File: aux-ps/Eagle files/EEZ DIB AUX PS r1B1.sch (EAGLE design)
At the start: 107 parts, among them IC1 AMC6821SDBQR, IC2 VIPer35L, IC3 TL431, J1 PF0030/PC, J2 SWEB 8094 AU/GN, Q1 BTA26-600, Q2 BTA26-600, Q3 2N7002, Q4 2N7002, Q5 IRLL2705PBF, Q6 2N7002, SW1 DF62J12S2AHQA, X1 39-28-1063, X2 39-30-1039, X3 ZL231-16KG, X4 22-23-2031, X5 22-23-2021

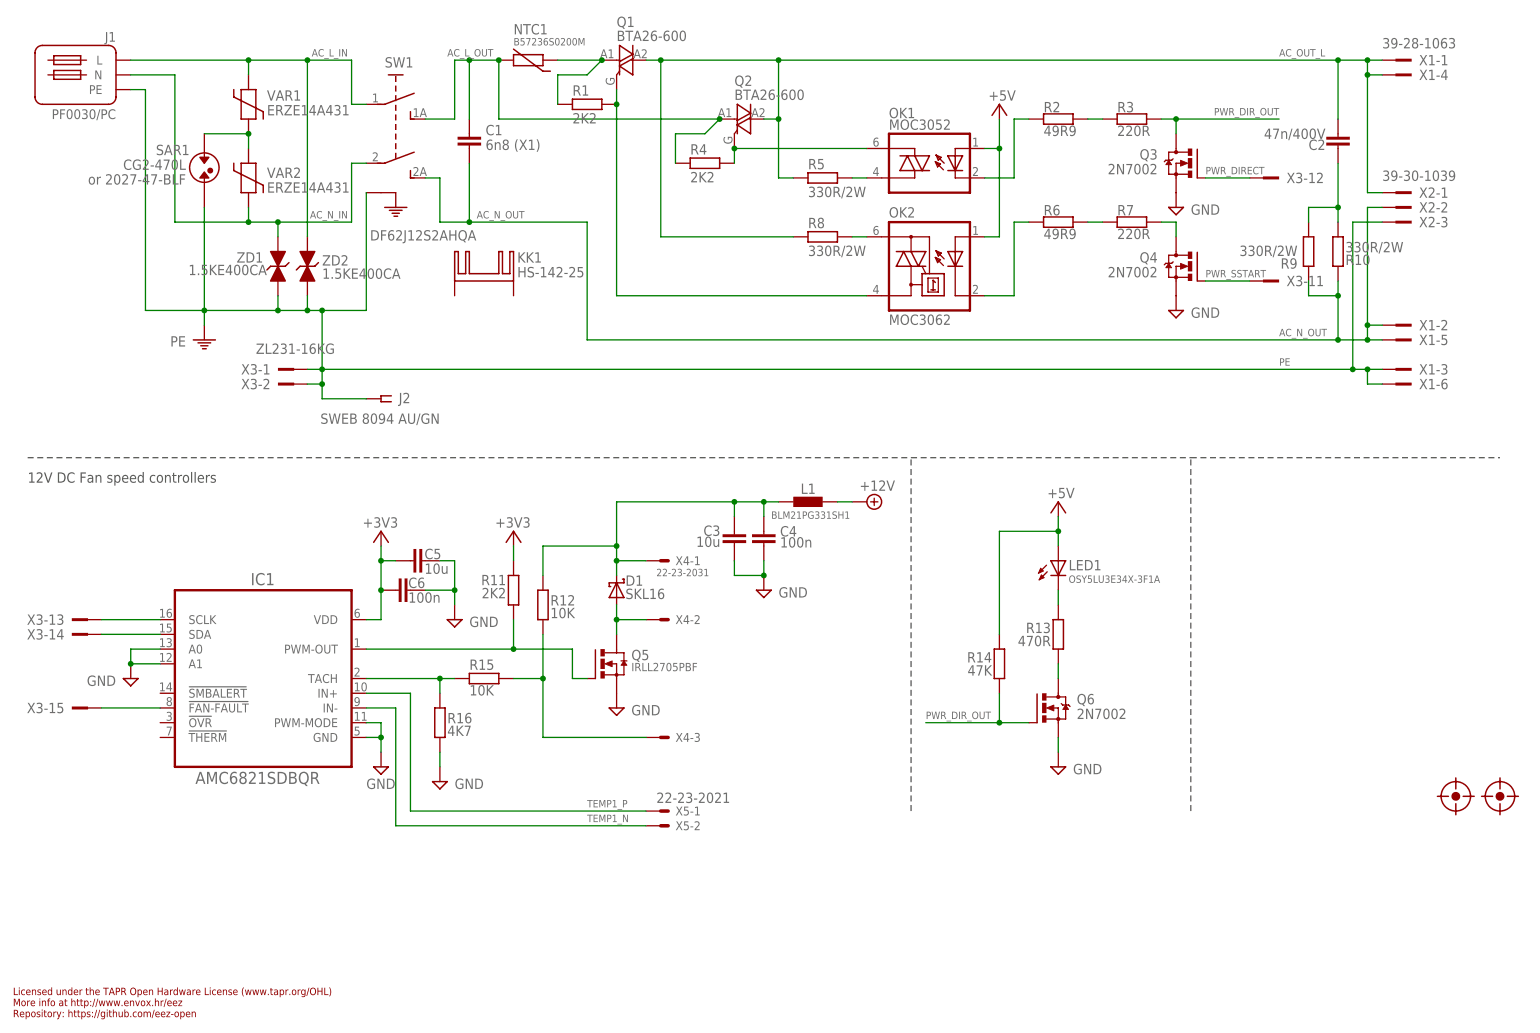
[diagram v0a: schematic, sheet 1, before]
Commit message: aux-ps BOM update, PE terminals added
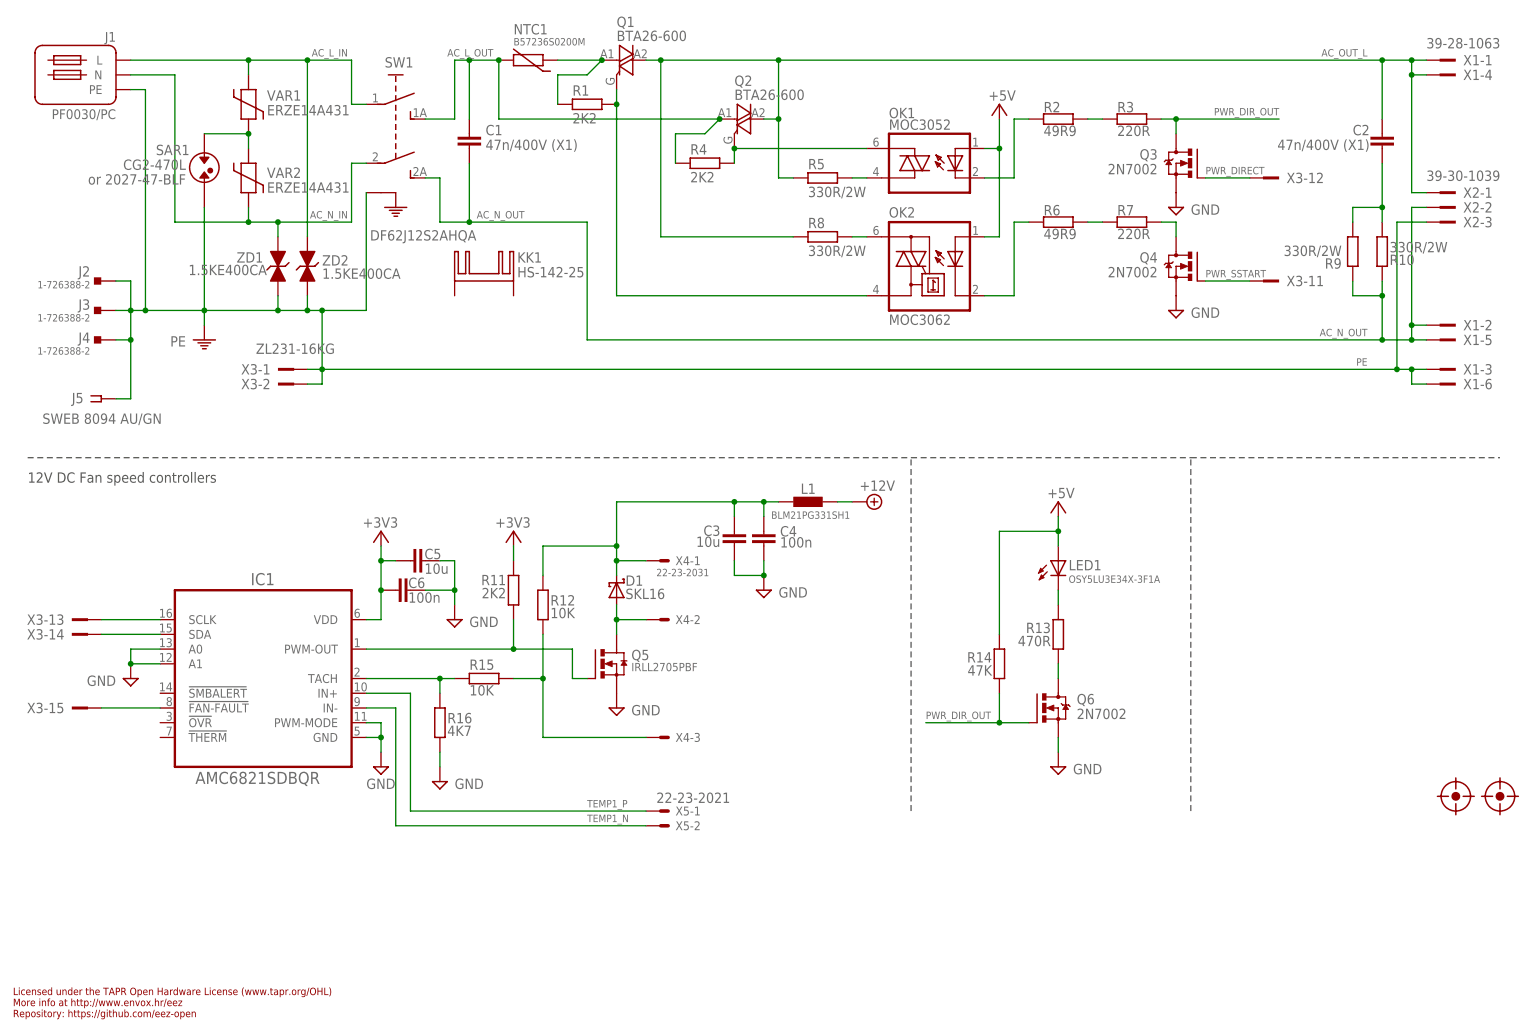
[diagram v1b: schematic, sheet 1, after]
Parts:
- added J3, J4: 1-726388-2, EEZ_connectors:PCB_TAB4.8MM
- added J5: SWEB 8094 AU/GN, EEZ_Lib1:BINDING_POSTCLIFF
- C1: value 6n8 (X1) -> 47n/400V (X1)
- C2: value 47n/400V -> 47n/400V (X1)
- C22: device rcl:C-EUC0805 -> rcl:C-EUC0603
- J2: value SWEB 8094 AU/GN -> 1-726388-2; device EEZ_Lib1:BINDING_POSTCLIFF -> EEZ_connectors:PCB_TAB4.8MM
- VAR1, VAR2: device EEZ_Lib1:VARISTOR -> EEZ_Lib1:VARISTOR-13
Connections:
- net PE: now also J2.P$1, J3.P$1, J4.P$1, J5.1; no longer J2.1
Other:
- moved on the sheet: C2, R10, R9, X1-1, X1-2, X1-3, X1-4, X1-5, X1-6, X2-1, X2-2, X2-3

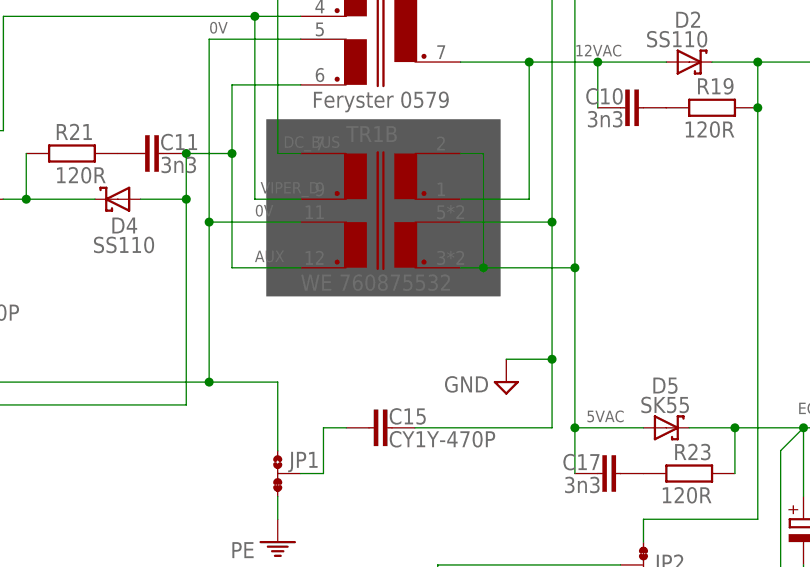
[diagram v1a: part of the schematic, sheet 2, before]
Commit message: PCB parts images added
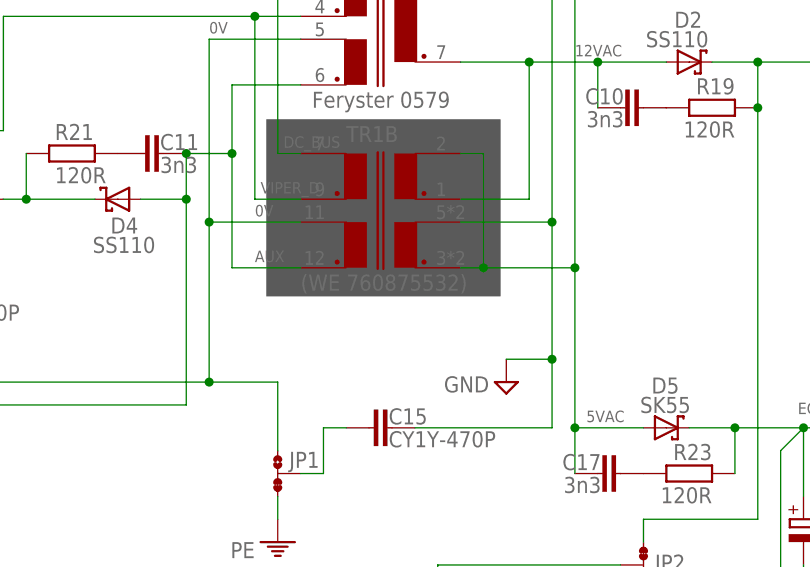
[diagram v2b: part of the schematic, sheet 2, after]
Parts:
- TR1B: value WE 760875532 -> (WE 760875532)
- X3: device EEZ_connectors:IDC-16PIN-F-ANGLED -> EEZ_connectors:IDC-16PIN-ANGLED
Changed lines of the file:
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@@
 <setting verticaltext="up"/>
 </settings>
-<grid distance="0.025" unitdist="inch" unit="inch" style="lines" multiple="4" display="no" altdistance="0.01" altunitdist="inch" altunit="inch"/>
+<grid distance="0.1" unitdist="inch" unit="inch" style="lines" multiple="1" display="no" altdistance="0.01" altunitdist="inch" altunit="inch"/>
 <layers>
 <layer number="1" name="Top" color="4" fill="1" visible="no" active="no"/>
@@
 <part name="VAR1" library="EEZ_Lib1" deviceset="VARISTOR" device="-13" value="ERZE14A431"/>
 <part name="C1" library="rcl" deviceset="C-EU" device="102-054X133" value="47n/400V (X1)"/>
-<part name="TR1B" library="EEZ_Lib1" deviceset="WE-UOST" device="" value="WE 760875532"/>
+<part name="TR1B" library="EEZ_Lib1" deviceset="WE-UOST" device="" value="(WE 760875532)"/>
 <part name="R8" library="rcl" deviceset="R-EU_" device="R2512" value="330R/2W"/>
 <part name="R5" library="rcl" deviceset="R-EU_" device="R2512" value="330R/2W"/>
@@
 <part name="SUPPLY72" library="supply2" deviceset="GND" device=""/>
 <part name="SUPPLY50" library="supply2" deviceset="GND" device=""/>
-<part name="X3" library="EEZ_connectors" deviceset="IDC-16PIN" device="-F-ANGLED" value="ZL231-16KG"/>
+<part name="X3" library="EEZ_connectors" deviceset="IDC-16PIN" device="-ANGLED" value="ZL231-16KG"/>
 <part name="SUPPLY1" library="supply2" deviceset="+12V" device=""/>
 <part name="+3V1" library="supply1" deviceset="+3V3" device=""/>

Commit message: minor changes in BOMs
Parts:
- added TP2: (no value), EEZ_Lib1:PCB_TEST_TABSHIELD
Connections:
- net GND: now also TP2.P$1
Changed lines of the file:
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@@
 <part name="J3" library="EEZ_connectors" deviceset="PCB_TAB" device="4.8MM" value="1-726388-2"/>
 <part name="J4" library="EEZ_connectors" deviceset="PCB_TAB" device="4.8MM" value="1-726388-2"/>
+<part name="TP2" library="EEZ_Lib1" deviceset="PCB_TEST_TAB" device="SHIELD"/>
 </parts>
 <sheets>
@@
 <attribute name="VALUE" x="206.883" y="91.9226" size="1.778" layer="96"/>
 </instance>
-<instance part="SUPPLY2" gate="GND" x="236.22" y="48.26" smashed="yes" rot="MR0">
-<attribute name="VALUE" x="238.76" y="44.45" size="1.778" layer="96" rot="MR0"/>
+<instance part="SUPPLY2" gate="GND" x="236.22" y="43.18" smashed="yes" rot="MR0">
+<attribute name="VALUE" x="238.76" y="39.37" size="1.778" layer="96" rot="MR0"/>
 </instance>
 <instance part="P+2" gate="1" x="236.22" y="111.76" smashed="yes">
@@
 <instance part="JP2" gate="G$1" x="187.96" y="91.44" smashed="yes" rot="R180">
 <attribute name="NAME" x="189.23" y="90.805" size="1.778" layer="95"/>
+</instance>
+<instance part="TP2" gate="G$1" x="243.84" y="48.26" smashed="yes">
+<attribute name="NAME" x="245.745" y="47.625" size="1.778" layer="95"/>
+<attribute name="VALUE" x="243.84" y="45.72" size="1.778" layer="96"/>
 </instance>
 </instances>
@@
 <pinref part="X3" gate="-8" pin="1"/>
 <wire x1="236.22" y1="55.88" x2="236.22" y2="53.34" width="0.1524" layer="91"/>
-<wire x1="236.22" y1="53.34" x2="236.22" y2="50.8" width="0.1524" layer="91"/>
+<wire x1="236.22" y1="53.34" x2="236.22" y2="48.26" width="0.1524" layer="91"/>
+<wire x1="236.22" y1="48.26" x2="236.22" y2="45.72" width="0.1524" layer="91"/>
 <wire x1="241.3" y1="55.88" x2="236.22" y2="55.88" width="0.1524" layer="91"/>
 <junction x="236.22" y="55.88"/>
@@
 <wire x1="241.3" y1="53.34" x2="236.22" y2="53.34" width="0.1524" layer="91"/>
 <junction x="236.22" y="53.34"/>
-</segment>
-<segment>
+<pinref part="TP2" gate="G$1" pin="P$1"/>
+<wire x1="241.3" y1="48.26" x2="236.22" y2="48.26" width="0.1524" layer="91"/>
+<junction x="236.22" y="48.26"/>
+</segment>
+<segment>
